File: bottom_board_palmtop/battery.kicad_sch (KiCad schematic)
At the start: 116 parts, among them J54 SH 2P, J7 Battery, J8 Battery, J9 Battery, Q11 HSM4313, Q18 2N7002DW-7-F, Q21 2N7002DW-7-F, Q3 CJ2305, Q4 2N7002DW-7-F, SW12 EVQPUL02K, SW2 ON/OFF, U24 SY6280AAAC, U25 SY6280AAAC, U36 AP62600SJ-7, U37 MIC2876-5.0, U39 AP2112K-3.3, U43 LP4034QVF, U44 TPS2121RUXR

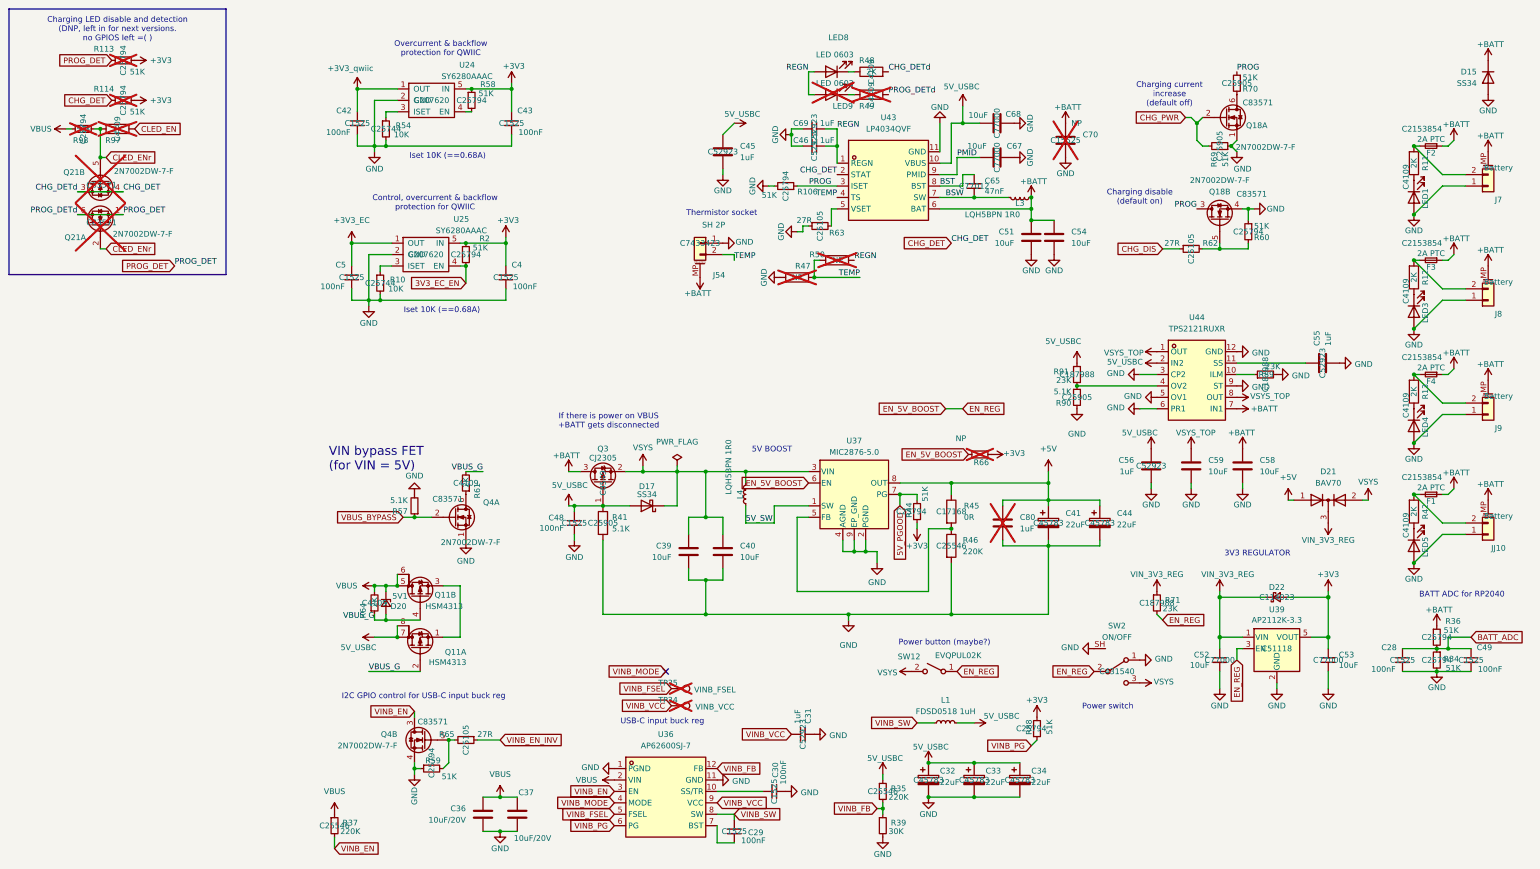
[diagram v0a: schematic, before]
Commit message: bottom_board_palmtop: JLC PCBA preparation; clarifying I2C addresses in use
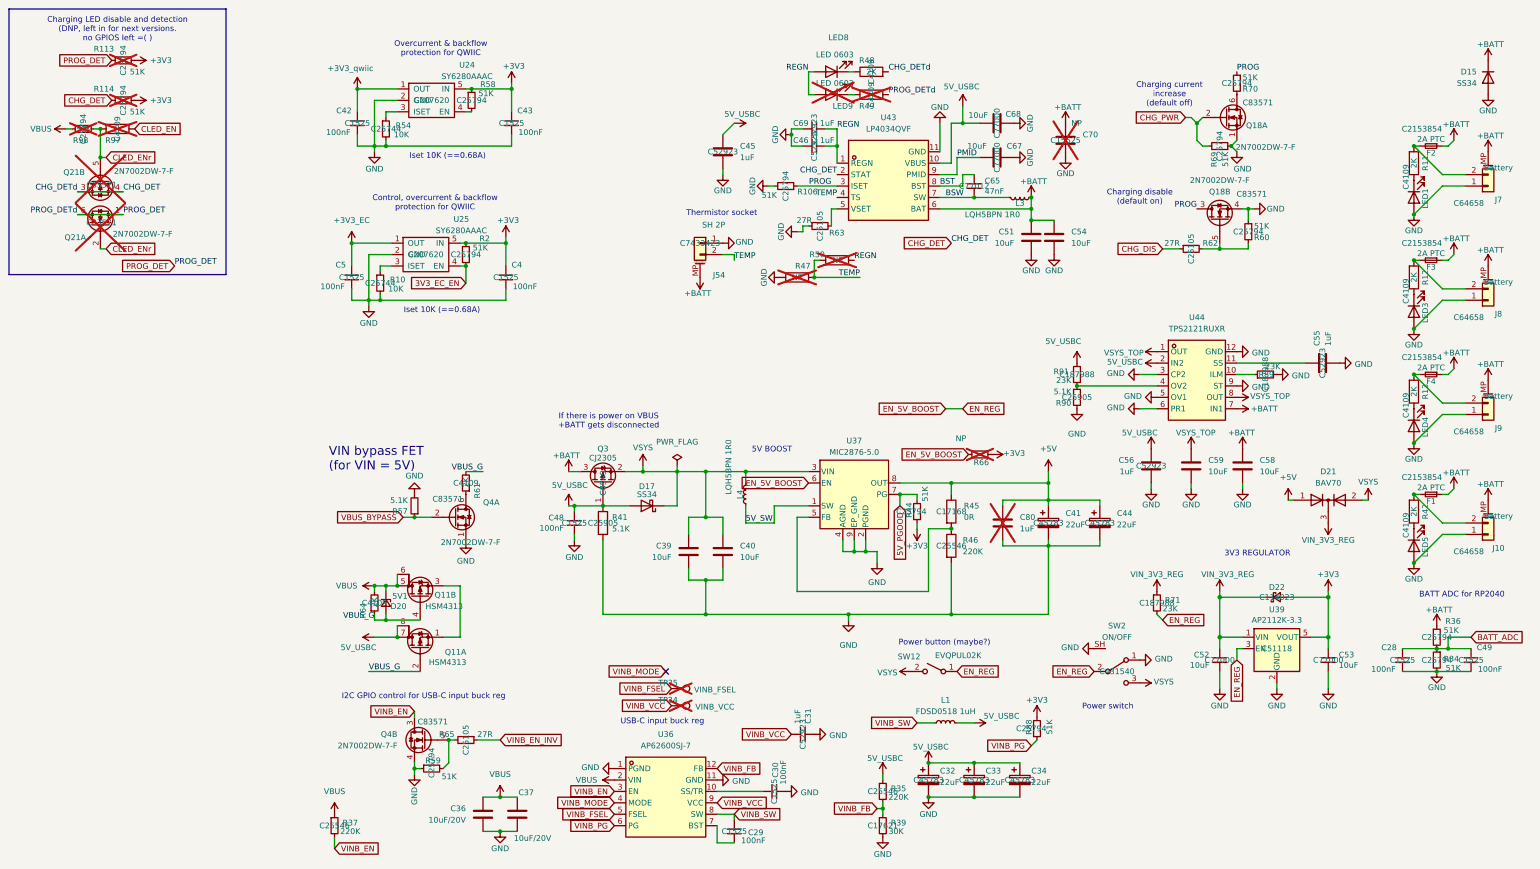
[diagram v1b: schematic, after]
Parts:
- J10: renamed from JJ10; LCSC Part (none) -> C64658
- J7, J8, J9: LCSC Part (none) -> C64658
- L1: LCSC Part (none) -> C7511322
- L3, L4: LCSC Part C576410 -> C337906
- LED1, LED3, LED4, LED5: value LED 0603 -> LED 0603 Orange
- R39: LCSC Part (none) -> C17621
- R57: LCSC Part (none) -> C25905
- R69, R70: LCSC Part C25905 -> C25794
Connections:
- net at U37.5 (NC): now also R45.2, R46.1
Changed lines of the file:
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@@
 			)
 		)
-		(property "LCSC Part" "C576410"
+		(property "LCSC Part" "C337906"
 			(at 107.95 115.57 90)
 			(effects
@@
 			)
 		)
-		(property "Value" "LED 0603"
+		(property "Value" "LED 0603 Orange"
 			(at 254 127.254 0)
 			(effects
@@
 			)
 		)
-		(property "Value" "LED 0603"
+		(property "Value" "LED 0603 Orange"
 			(at 254 49.784 0)
 			(effects
@@
 			)
 		)
+		(property "LCSC Part" "C25905"
+			(at 34.29 118.11 0)
+			(effects
+				(font
+					(size 1.27 1.27)
+				)
+				(hide yes)
+			)
+		)
 		(pin "1"
 		)
@@
 			)
 		)
-		(property "LCSC Part" ""
+		(property "LCSC Part" "C17621"
 			(at 138.43 189.23 0)
 			(effects
@@
 			)
 		)
-		(property "LCSC Part" "C25905"
+		(property "LCSC Part" "C25794"
 			(at 213.36 38.1 0)
 			(effects
@@
 			)
 		)
-		(property "LCSC Part" "C25905"
+		(property "LCSC Part" "C25794"
 			(at 217.17 24.13 0)
 			(effects
@@
 			)
 		)
+		(property "LCSC Part" "C7511322"
+			(at 152.4 166.37 90)
+			(effects
+				(font
+					(size 1.27 1.27)
+				)
+				(hide yes)
+			)
+		)
 		(pin "1"
 		)
@@
 			)
 		)
-		(property "Value" "LED 0603"
+		(property "Value" "LED 0603 Orange"
 			(at 254 100.584 0)
 			(effects
@@
 			)
 		)
-		(property "LCSC Part" ""
+		(property "LCSC Part" "C64658"
 			(at 268.732 101.6 0)
 			(effects
@@
 		(on_board yes)
 		(dnp no)
-		(property "Reference" "JJ10"
+		(property "Reference" "J10"
 			(at 275.336 127.508 0)
 			(effects
@@
 			)
 		)
-		(property "LCSC Part" ""
+		(property "LCSC Part" "C64658"
 			(at 268.732 128.27 0)
 			(effects
@@
 			(project "bottom_board_palmtop"
 				(path "/8978b49f-2e56-47e1-8d7c-c31ed8b7a8ae/302b4957-4a57-4c5f-969c-c84eae9303f5"
-					(reference "JJ10")
+					(reference "J10")
 					(unit 1)
 				)
@@
 			)
 		)
-		(property "LCSC Part" ""
+		(property "LCSC Part" "C64658"
 			(at 268.732 50.8 0)
 			(effects
@@
 			)
 		)
-		(property "Value" "LED 0603"
+		(property "Value" "LED 0603 Orange"
 			(at 254 75.184 0)
 			(effects
@@
 			)
 		)
-		(property "LCSC Part" "C576410"
+		(property "LCSC Part" "C337906"
 			(at 168.91 49.53 90)
 			(effects
@@
 			)
 		)
-		(property "LCSC Part" ""
+		(property "LCSC Part" "C64658"
 			(at 268.732 76.2 0)
 			(effects

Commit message: changing JST-SH 2p connectors to vertical, poking board art around and adding more
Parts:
- J54: footprint Connector_JST:JST_SH_SM02B-SRSS-TB_1x02-1MP_P1.00mm_Horizontal -> Connector_JST:JST_SH_BM02B-SRSS-TB_1x02-1MP_P1.00mm_Vertical
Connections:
- net at U37.5 (NC): now also R45.2, R46.1
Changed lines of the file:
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@@
 			)
 		)
-		(property "Footprint" "Connector_JST:JST_SH_SM02B-SRSS-TB_1x02-1MP_P1.00mm_Horizontal"
+		(property "Footprint" "Connector_JST:JST_SH_BM02B-SRSS-TB_1x02-1MP_P1.00mm_Vertical"
 			(at 97.79 59.69 0)
 			(effects
